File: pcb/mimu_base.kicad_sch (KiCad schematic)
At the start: 16 parts, among them J1 OPT, SW1 SW_Push, U1 PC817, U2 ATTINY88AU

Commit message: First layout
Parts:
- C1, C2: footprint Capacitor_SMD:C_0805_2012Metric_Pad1.15x1.40mm_HandSolder -> Capacitor_SMD:C_1206_3216Metric_Pad1.33x1.80mm_HandSolder
- D2: renamed from D?; footprint (none) -> LED_THT:LED_D3.0mm-3
- ISP1: footprint Connector_PinHeader_2.54mm:PinHeader_2x03_P2.54mm_Vertical -> ProjectLibrary:PinHeader_2x03_P2.54mm_Vertical_pogo
- R2: renamed from R5; footprint Capacitor_SMD:C_1206_3216Metric_Pad1.33x1.80mm_HandSolder -> Resistor_SMD:R_1206_3216Metric_Pad1.30x1.75mm_HandSolder
- gave numbers to parts that had none: 4
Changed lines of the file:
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@@
       (effects (font (size 1.27 1.27)) (justify right))
     )
-    (property "Footprint" "Connector_PinHeader_2.54mm:PinHeader_2x03_P2.54mm_Vertical" (id 2) (at 186.69 107.95 90)
+    (property "Footprint" "ProjectLibrary:PinHeader_2x03_P2.54mm_Vertical_pogo" (id 2) (at 186.69 107.95 90)
       (effects (font (size 1.27 1.27)) hide)
     )
@@
       (effects (font (size 1.27 1.27)) (justify left))
     )
-    (property "Footprint" "Capacitor_SMD:C_0805_2012Metric_Pad1.15x1.40mm_HandSolder" (id 2) (at 158.4452 148.59 0)
+    (property "Footprint" "Capacitor_SMD:C_1206_3216Metric_Pad1.33x1.80mm_HandSolder" (id 2) (at 158.4452 148.59 0)
       (effects (font (size 1.27 1.27)) hide)
     )
@@
       (effects (font (size 1.27 1.27)) (justify left))
     )
-    (property "Footprint" "Capacitor_SMD:C_0805_2012Metric_Pad1.15x1.40mm_HandSolder" (id 2) (at 171.1452 148.59 0)
+    (property "Footprint" "Capacitor_SMD:C_1206_3216Metric_Pad1.33x1.80mm_HandSolder" (id 2) (at 171.1452 148.59 0)
       (effects (font (size 1.27 1.27)) hide)
     )
@@
   (symbol (lib_id "Device:R") (at 57.15 163.83 0) (unit 1)
     (in_bom yes) (on_board yes)
-    (property "Reference" "R5" (id 0) (at 58.928 162.6616 0)
+    (property "Reference" "R2" (id 0) (at 58.928 162.6616 0)
       (effects (font (size 1.27 1.27)) (justify left))
     )
@@
       (effects (font (size 1.27 1.27)) (justify left))
     )
-    (property "Footprint" "Capacitor_SMD:C_1206_3216Metric_Pad1.33x1.80mm_HandSolder" (id 2) (at 55.372 163.83 90)
+    (property "Footprint" "Resistor_SMD:R_1206_3216Metric_Pad1.30x1.75mm_HandSolder" (id 2) (at 55.372 163.83 90)
       (effects (font (size 1.27 1.27)) hide)
     )
@@
   (symbol (lib_id "power:VCC") (at 66.04 34.29 0) (unit 1)
     (in_bom yes) (on_board yes)
-    (property "Reference" "#PWR?" (id 0) (at 66.04 38.1 0)
+    (property "Reference" "#PWR0112" (id 0) (at 66.04 38.1 0)
       (effects (font (size 1.27 1.27)) hide)
     )
@@
   (symbol (lib_id "power:VCC") (at 99.06 34.29 0) (unit 1)
     (in_bom yes) (on_board yes)
-    (property "Reference" "#PWR?" (id 0) (at 99.06 38.1 0)
+    (property "Reference" "#PWR0108" (id 0) (at 99.06 38.1 0)
       (effects (font (size 1.27 1.27)) hide)
     )
@@
   (symbol (lib_id "Device:R") (at 88.9 64.77 90) (unit 1)
     (in_bom yes) (on_board yes) (fields_autoplaced)
-    (property "Reference" "R?" (id 0) (at 88.9 60.0542 90))
+    (property "Reference" "R5" (id 0) (at 88.9 60.0542 90))
     (property "Value" "12R" (id 1) (at 88.9 62.5911 90))
     (property "Footprint" "Resistor_SMD:R_1206_3216Metric_Pad1.30x1.75mm_HandSolder" (id 2) (at 88.9 66.548 90)
@@
   (symbol (lib_id "custom:AD5258") (at 66.04 73.66 0) (unit 1)
     (in_bom yes) (on_board yes) (fields_autoplaced)
-    (property "Reference" "U?" (id 0) (at 68.0594 49.6402 0)
+    (property "Reference" "U4" (id 0) (at 68.0594 49.6402 0)
       (effects (font (size 1.27 1.27)) (justify left))
     )
@@
   (symbol (lib_id "Transistor_FET:BSS84") (at 101.6 46.99 180) (unit 1)
     (in_bom yes) (on_board yes) (fields_autoplaced)
-    (property "Reference" "Q?" (id 0) (at 96.3931 46.1553 0)
+    (property "Reference" "Q1" (id 0) (at 96.3931 46.1553 0)
       (effects (font (size 1.27 1.27)) (justify left))
     )
@@
   (symbol (lib_id "Device:R") (at 110.49 64.77 90) (unit 1)
     (in_bom yes) (on_board yes) (fields_autoplaced)
-    (property "Reference" "R?" (id 0) (at 110.49 60.0542 90))
+    (property "Reference" "R6" (id 0) (at 110.49 60.0542 90))
     (property "Value" "68R" (id 1) (at 110.49 62.5911 90))
     (property "Footprint" "Resistor_SMD:R_1206_3216Metric_Pad1.30x1.75mm_HandSolder" (id 2) (at 110.49 66.548 90)
@@
   (symbol (lib_id "power:VCC") (at 73.66 85.09 0) (unit 1)
     (in_bom yes) (on_board yes)
-    (property "Reference" "#PWR?" (id 0) (at 73.66 88.9 0)
+    (property "Reference" "#PWR0114" (id 0) (at 73.66 88.9 0)
       (effects (font (size 1.27 1.27)) hide)
     )
@@
   (symbol (lib_id "power:GND") (at 63.5 85.09 0) (unit 1)
     (in_bom yes) (on_board yes)
-    (property "Reference" "#PWR?" (id 0) (at 63.5 91.44 0)
+    (property "Reference" "#PWR0113" (id 0) (at 63.5 91.44 0)
       (effects (font (size 1.27 1.27)) hide)
     )
@@
   (symbol (lib_id "power:GND") (at 81.28 76.2 0) (unit 1)
     (in_bom yes) (on_board yes)
-    (property "Reference" "#PWR?" (id 0) (at 81.28 82.55 0)
+    (property "Reference" "#PWR0110" (id 0) (at 81.28 82.55 0)
       (effects (font (size 1.27 1.27)) hide)
     )
@@
   (symbol (lib_id "power:VCC") (at 81.28 34.29 0) (unit 1)
     (in_bom yes) (on_board yes)
-    (property "Reference" "#PWR?" (id 0) (at 81.28 38.1 0)
+    (property "Reference" "#PWR0111" (id 0) (at 81.28 38.1 0)
       (effects (font (size 1.27 1.27)) hide)
     )
@@
   (symbol (lib_id "Device:LED_Dual_KAK") (at 54.61 175.26 90) (unit 1)
     (in_bom yes) (on_board yes) (fields_autoplaced)
-    (property "Reference" "D?" (id 0) (at 59.944 174.3618 90)
+    (property "Reference" "D2" (id 0) (at 59.944 174.3618 90)
       (effects (font (size 1.27 1.27)) (justify right))
     )
@@
       (effects (font (size 1.27 1.27)) (justify right))
     )
-    (property "Footprint" "" (id 2) (at 54.61 173.99 0)
-      (effects (font (size 1.27 1.27)) hide)
-    )
+    (property "Footprint" "LED_THT:LED_D3.0mm-3" (id 2) (at 54.61 173.99 0))
     (property "Datasheet" "~" (id 3) (at 54.61 173.99 0)
       (effects (font (size 1.27 1.27)) hide)

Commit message: Minor PCB updates
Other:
- moved on the sheet: ISP1

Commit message: Added Switch for drive_fallback mode
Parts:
- added SW2: In case mosfet does not work as expected, Jumper:SolderJumper-2_P1.3mm_Open_TrianglePad1.0x1.5mm, symbol Switch:SW_DPST_x2
- ISP1: now left out of the parts list
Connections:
- net MUTE_DRIVE: now also SW2.1 (A)
- net at Q1.3 (D), R5.2, R6.1: now also SW2.2 (B)
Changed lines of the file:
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@@
   (junction (at 152.4 45.72) (diameter 0) (color 0 0 0 0)
   )
+  (junction (at 116.84 46.99) (diameter 0) (color 0 0 0 0)
+  )
   (junction (at 161.29 45.72) (diameter 0) (color 0 0 0 0)
   )
@@
   )
   (junction (at 53.34 127) (diameter 0) (color 0 0 0 0)
+  )
+  (junction (at 99.06 52.705) (diameter 0) (color 0 0 0 0)
   )
   (junction (at 53.34 71.12) (diameter 0) (color 0 0 0 0)
@@
     (stroke (width 0) (type default) (color 0 0 0 0))
   )
+  (wire (pts (xy 116.84 46.99) (xy 116.84 52.705))
+    (stroke (width 0) (type default) (color 0 0 0 0))
+  )
   (wire (pts (xy 247.65 102.87) (xy 255.27 102.87))
     (stroke (width 0) (type default) (color 0 0 0 0))
@@
     (stroke (width 0) (type default) (color 0 0 0 0))
   )
+  (wire (pts (xy 99.06 52.705) (xy 99.06 64.77))
+    (stroke (width 0) (type default) (color 0 0 0 0))
+  )
   (wire (pts (xy 157.48 151.13) (xy 157.48 148.59))
     (stroke (width 0) (type default) (color 0 0 0 0))
@@
     (stroke (width 0) (type default) (color 0 0 0 0))
   )
+  (wire (pts (xy 99.06 52.705) (xy 106.68 52.705))
+    (stroke (width 0) (type default) (color 0 0 0 0))
+  )
   (wire (pts (xy 207.01 124.46) (xy 207.01 81.28))
     (stroke (width 0) (type default) (color 0 0 0 0))
@@
     (stroke (width 0) (type default) (color 0 0 0 0))
   )
-  (wire (pts (xy 99.06 52.07) (xy 99.06 64.77))
+  (wire (pts (xy 99.06 52.07) (xy 99.06 52.705))
     (stroke (width 0) (type default) (color 0 0 0 0))
   )
@@
   )
   (text "AD1 = 0   0b0011000\nAD1 = 1   0b1001100\n\nAD0 adds  0b0000010"
-    (at 49.53 76.2 180)
+    (at 49.53 76.2 0)
     (effects (font (size 1.27 1.27)) (justify right bottom))
   )
@@
   )
   (symbol (lib_id "Connector:AVR-ISP-6") (at 193.04 83.82 0) (unit 1)
-    (in_bom yes) (on_board yes)
+    (in_bom no) (on_board yes)
     (property "Reference" "ISP1" (id 0) (at 184.6834 81.3816 0)
       (effects (font (size 1.27 1.27)) (justify right))
@@
     (pin "1")
   )
+  (symbol (lib_id "Switch:SW_DPST_x2") (at 111.76 52.705 180) (unit 1)
+    (in_bom yes) (on_board yes)
+    (property "Reference" "SW2" (id 0) (at 111.125 50.8 0))
+    (property "Value" "In case mosfet does not work as expected" (id 1) (at 111.76 55.88 0)
+      (effects (font (size 0.57 0.57)))
+    )
+    (property "Footprint" "Jumper:SolderJumper-2_P1.3mm_Open_TrianglePad1.0x1.5mm" (id 2) (at 111.76 52.705 0)
+      (effects (font (size 1.27 1.27)) hide)
+    )
+    (property "Datasheet" "~" (id 3) (at 111.76 52.705 0)
+      (effects (font (size 1.27 1.27)) hide)
+    )
+    (pin "1")
+    (pin "2")
+    (pin "3")
+    (pin "4")
+  )
   (symbol (lib_id "power:VCC") (at 66.04 34.29 0) (unit 1)

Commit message: Fixed Issue #6 by mirroring TOF connector pins
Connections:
- net GND: now also SENS1.3 (GND); no longer SENS1.2 (GND)
- net SCL: now also SENS1.2 (SCL); no longer SENS1.3 (SCL)
- net SDA: now also SENS1.1 (SDA); no longer SENS1.4 (SDA)
- net VCC: now also SENS1.4 (VCC); no longer SENS1.1 (VCC)
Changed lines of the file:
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@@
-    (stroke (width 0) (type default) (color 0 0 0 0))
-  )
-  (wire (pts (xy 261.62 40.64) (xy 259.08 40.64))
     (stroke (width 0) (type default) (color 0 0 0 0))
   )
@@
   )
   (wire (pts (xy 73.66 86.36) (xy 73.66 85.09))
+    (stroke (width 0) (type default) (color 0 0 0 0))
+  )
+  (wire (pts (xy 259.08 40.64) (xy 261.62 40.64))
     (stroke (width 0) (type default) (color 0 0 0 0))
   )
@@
   (symbol (lib_id "mimu_phantom-rescue:Conn_TOF_flipped-custom") (at 254 38.1 180) (unit 1)
     (in_bom yes) (on_board yes)
-    (property "Reference" "SENS1" (id 0) (at 256.0828 27.305 0))
-    (property "Value" "Sens" (id 1) (at 256.0828 29.6164 0))
+    (property "Reference" "SENS1" (id 0) (at 251.9172 48.895 0))
+    (property "Value" "Sens" (id 1) (at 251.9172 46.5836 0))
     (property "Footprint" "Connector_PinHeader_2.54mm:PinHeader_1x04_P2.54mm_Vertical" (id 2) (at 254 38.1 0)
       (effects (font (size 1.27 1.27)) hide)
@@
       (effects (font (size 1.27 1.27)) hide)
     )
+    (pin "4")
+    (pin "3")
+    (pin "2")
     (pin "1")
-    (pin "2")
-    (pin "3")
-    (pin "4")
   )
   (symbol (lib_id "mimu_phantom-rescue:H11F1M-custom") (at 130.81 67.31 0) (unit 1)

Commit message: Removed some Debug writes
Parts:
- C1, C2: value 0.1uF -> (none); footprint Capacitor_SMD:C_1206_3216Metric_Pad1.33x1.80mm_HandSolder -> (none)
- D2: value LED_Dual_KAK -> (none); footprint LED_THT:LED_D3.0mm-3 -> (none)
- INPUT1: value XLR3 -> (none); footprint Connector_PinHeader_2.54mm:PinHeader_1x03_P2.54mm_Vertical -> (none)
- ISP1: value AVR-ISP-6 -> (none); footprint ProjectLibrary:PinHeader_2x03_P2.54mm_Vertical_pogo -> (none)
- J1: value OPT -> (none); footprint Connector_PinHeader_1.27mm:PinHeader_1x05_P1.27mm_Vertical -> (none)
- Q1: value BSS84 -> (none); footprint Package_TO_SOT_SMD:SOT-23 -> (none)
- R1: value 390R -> (none); footprint Capacitor_SMD:C_1206_3216Metric_Pad1.33x1.80mm_HandSolder -> (none)
- R2: value 390R -> (none); footprint Resistor_SMD:R_1206_3216Metric_Pad1.30x1.75mm_HandSolder -> (none)
- R5: value 12R -> (none); footprint Resistor_SMD:R_1206_3216Metric_Pad1.30x1.75mm_HandSolder -> (none)
- R6: value 68R -> (none); footprint Resistor_SMD:R_1206_3216Metric_Pad1.30x1.75mm_HandSolder -> (none)
- SENS1: value Sens -> (none); footprint Connector_PinHeader_2.54mm:PinHeader_1x04_P2.54mm_Vertical -> (none)
- SW1: value SW_Push -> (none); footprint digikey:Switch_Tactile_SMD_6x6mm_PTS645 -> (none)
- SW2: value In case mosfet does not work as expected -> (none); footprint Jumper:SolderJumper-2_P1.3mm_Open_TrianglePad1.0x1.5mm -> (none)
- U1: value PC817 -> (none); footprint custom:DIP-4_bubble_W7.62mm -> (none)
- U2: value ATTINY88AU -> (none); footprint Package_QFP:TQFP-32_7x7mm_P0.8mm -> (none)
- U4: value AD5258 -> (none); footprint Package_SO:MSOP-10_3x3mm_P0.5mm -> (none)

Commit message: Test with using the other optocoupler that needs less current
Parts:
- C1, C2: value (none) -> 0.1uF; footprint (none) -> Capacitor_SMD:C_1206_3216Metric_Pad1.33x1.80mm_HandSolder
- D2: value (none) -> LED_Dual_KAK; footprint (none) -> LED_THT:LED_D3.0mm-3
- INPUT1: value (none) -> XLR3; footprint (none) -> Connector_PinHeader_2.54mm:PinHeader_1x03_P2.54mm_Vertical
- ISP1: value (none) -> AVR-ISP-6; footprint (none) -> ProjectLibrary:PinHeader_2x03_P2.54mm_Vertical_pogo
- J1: value (none) -> OPT; footprint (none) -> Connector_PinHeader_1.27mm:PinHeader_1x05_P1.27mm_Vertical
- Q1: value (none) -> BSS84; footprint (none) -> Package_TO_SOT_SMD:SOT-23
- R1: value (none) -> 390R; footprint (none) -> Capacitor_SMD:C_1206_3216Metric_Pad1.33x1.80mm_HandSolder
- R2: value (none) -> 390R; footprint (none) -> Resistor_SMD:R_1206_3216Metric_Pad1.30x1.75mm_HandSolder
- R5: value (none) -> 0R; footprint (none) -> Resistor_SMD:R_1206_3216Metric_Pad1.30x1.75mm_HandSolder
- R6: value (none) -> 300R; footprint (none) -> Resistor_SMD:R_1206_3216Metric_Pad1.30x1.75mm_HandSolder
- SENS1: value (none) -> Sens; footprint (none) -> Connector_PinHeader_2.54mm:PinHeader_1x04_P2.54mm_Vertical
- SW1: value (none) -> SW_Push; footprint (none) -> digikey:Switch_Tactile_SMD_6x6mm_PTS645
- SW2: value (none) -> In case mosfet does not work as expected; footprint (none) -> Jumper:SolderJumper-2_P1.3mm_Open_TrianglePad1.0x1.5mm
- U1: value (none) -> NSL-32SR3; footprint (none) -> custom:DIP-4_bubble_W7.62mm
- U2: value (none) -> ATTINY88AU; footprint (none) -> Package_QFP:TQFP-32_7x7mm_P0.8mm
- U4: value (none) -> AD5258 - 1k; footprint (none) -> Package_SO:MSOP-10_3x3mm_P0.5mm
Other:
- note added: "330R with 3.3kR is 300 Ohm equivalent parallel"
- note added: "I_Fon = 5-25mA V_fwd =~ 1.2v ??? Unspecified Tested OK at 2mA, best between 3mA to 8mA"
- note added: "I_max(digipot) = 20mA R_wiper is ~ 20Ohm so + 300Ohm -> 10.3mA"
- note added: "TODO: Mosfet not needed anymore"
- note added: "Todo: Mosfet on digipot:A to conserve power?"
- note added: "target: 10mA actual: 11mA"
- note removed: "I_Fon = 20-50mA V_fwd =~ 1.2v "good enough" at ~25mA, perhaps 30mA"
- note removed: "I_max = 20mA (12R + 68R) = 80R -> 26mA But: R_wiper is ~ 20Ohm, so correct"
- note removed: "target: 30mA actual: 30.9mA"

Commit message: Initial playarounds for rheostat mode
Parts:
- removed R5: 0R, Resistor_SMD:R_1206_3216Metric_Pad1.30x1.75mm_HandSolder, symbol Device:R
- added C4: 0.1 nF, Resistor_SMD:R_1206_3216Metric_Pad1.30x1.75mm_HandSolder, symbol Device:C
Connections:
- net GND: now also C4.2; no longer U4.9 (B)
- net VCC: no longer U4.10 (A)
- net at R6.2, U1.1: now also C4.1
- net at Q1.3 (D), SW2.2 (B): now also U4.10 (A); no longer R6.1
- net at U4.1 (W): now also R6.1
- no-connect marks 13 -> 14
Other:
- note added: "R_Digipot_"off" = 1000 + 20R wiper => Least current = 3.3v / 1020R + 300R = 2.5 mA !"
- note added: "Target max slope off->on = 500us RC 300R -> magic -> 0.1 nF"
- note removed: "TODO: Mosfet not needed anymore"
- note removed: "Todo: Mosfet on digipot:A to conserve power?"
- moved on the sheet: INPUT1, ISP1, Q1, R6, SW2A, U1, U4

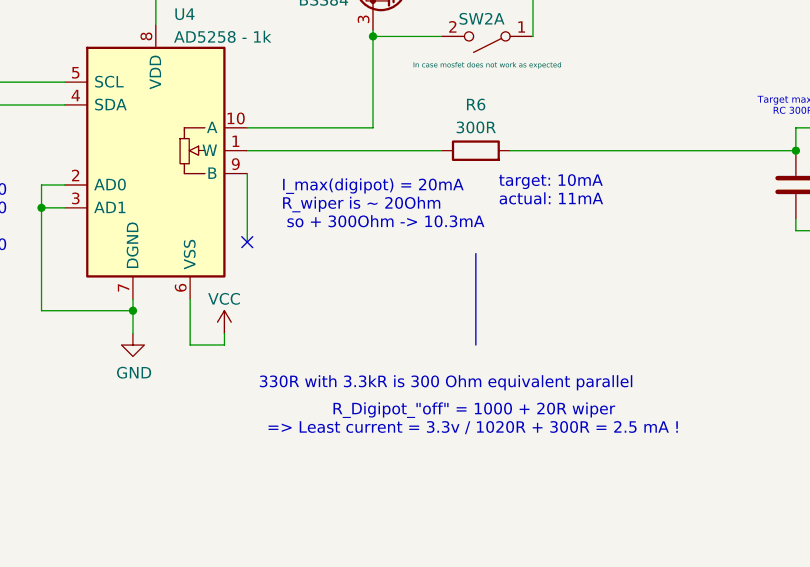
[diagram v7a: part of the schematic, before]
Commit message: Added emphasis on having less VCC. 3v work fine, perhaps even less.
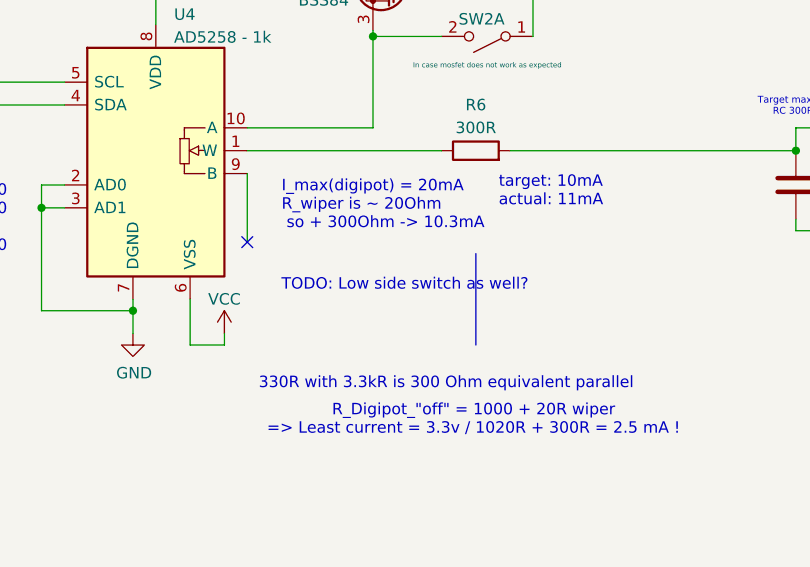
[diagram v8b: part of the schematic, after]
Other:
- note added: "TODO: Low side switch as well?"
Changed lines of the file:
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@@
+		)
+	)
+	(text "TODO: Low side switch as well?"
+		(exclude_from_sim no)
+		(at 82.296 69.596 0)
+		(effects
+			(font
+				(size 1.27 1.27)
+			)
 		)
 	)
